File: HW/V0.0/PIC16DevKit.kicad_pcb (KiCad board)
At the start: 2 copper layers, 0 parts

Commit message: PIC16-DevKit-SCH-877 schematic update 5
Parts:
- added C1: 470uF, SAMPI:CAP_ELEC-8.3x8.3-DIA8.0, F.Cu at (77.6, 134.1)
- added C10: 10uF, SAMPI:CAP0603, F.Cu at (62.0, 146.1)
- added C11: 10uF, SAMPI:CAP0603, F.Cu at (65.7, 130.5)
- added C12: 22pF, SAMPI:CAP0603, F.Cu at (65.7, 133.1)
- added C13: 10uF, SAMPI:CAP0603, F.Cu at (65.7, 135.7)
- added C14: 100nF, SAMPI:CAP0603, F.Cu at (65.7, 138.3)
- added C15: 22pF, SAMPI:CAP0603, F.Cu at (89.7, 98.9)
- added C16: 22pF, SAMPI:CAP0603, F.Cu at (89.7, 101.5)
- added C17: 100nF, SAMPI:CAP0603, F.Cu at (89.7, 104.1)
- added C18: 100nF, SAMPI:CAP0603, F.Cu at (89.7, 106.7)
- added C19: 10uF, SAMPI:CAP0603, F.Cu at (89.7, 109.3)
- added C2: 220uF, SAMPI:CAP1411, F.Cu at (86.9, 144.4)
- added C20: 100nF, SAMPI:CAP0603, F.Cu at (93.4, 98.9)
- added C21: 10uF, SAMPI:CAP0603, F.Cu at (93.4, 101.5)
- added C22: 100nF, SAMPI:CAP0603, F.Cu at (99.3, 120.6)
- added C23: 100nF, SAMPI:CAP0603, F.Cu at (99.3, 123.2)
- added C24: 100nF, SAMPI:CAP0603, F.Cu at (99.3, 125.8)
- added C25: 100nF, SAMPI:CAP0603, F.Cu at (99.3, 128.5)
- added C26: 100nF, SAMPI:CAP0603, F.Cu at (99.3, 131.1)
- added C27: 10uF, SAMPI:CAP0603, F.Cu at (99.3, 133.7)
- added C28: 100nF, SAMPI:CAP0603, F.Cu at (99.3, 136.3)
- added C29: 10uF, SAMPI:CAP0603, F.Cu at (103.0, 120.6)
- added C3: 10uF/16V, SAMPI:CAP1206, F.Cu at (92.8, 140.3)
- added C30: 100nF, SAMPI:CAP0603, F.Cu at (103.0, 123.2)
- added C31: 100nF, SAMPI:CAP0603, F.Cu at (103.0, 125.8)
- added C32: 100nF, SAMPI:CAP0603, F.Cu at (103.0, 128.5)
- added C33: 100nF, SAMPI:CAP0603, F.Cu at (103.0, 131.1)
- added C34: 100nF, SAMPI:CAP0603, F.Cu at (103.0, 133.7)
- added C35: 100nF, SAMPI:CAP0603, F.Cu at (103.0, 136.3)
- added C36: 100nF, SAMPI:CAP0603, F.Cu at (106.7, 120.6)
- added C37: 100nF, SAMPI:CAP0603, F.Cu at (106.7, 123.2)
- added C4: 100nF, SAMPI:CAP0603, F.Cu at (62.0, 130.5)
- added C5: 100nF, SAMPI:CAP0603, F.Cu at (62.0, 133.1)
- added C6: 100nF, SAMPI:CAP0603, F.Cu at (62.0, 135.7)
- added C7: 10uF, SAMPI:CAP0603, F.Cu at (62.0, 138.3)
- added C8: 10uF, SAMPI:CAP0603, F.Cu at (62.0, 140.9)
- added C9: 10uF, SAMPI:CAP0603, F.Cu at (62.0, 143.5)
- added D1: 5V1, SAMPI:SOD80C-LL34, F.Cu at (86.9, 127.6)
- added D2: 200mA/0.2VF, Liem:SOD-123FL, F.Cu at (87.1, 136.5)
- added D3: TVS 5V, Triet_KiCAD_Fprint:SOT-143-TVS, F.Cu at (92.7, 136.8)
- added D4: 200mA/0.2VF, Liem:SOD-123FL, F.Cu at (87.1, 140.1)
- added D5: ULED, SAMPI:LED0603, F.Cu at (93.4, 104.1)
- added D6: TARGET, SAMPI:LED0603, F.Cu at (106.7, 125.8)
- added D7: BUSY, SAMPI:LED0603, F.Cu at (106.7, 128.5)
- added F1: 1A, SAMPI:FUSE1812, F.Cu at (80.3, 121.0)
- added F2: 750mA, SAMPI:FUSE1812, F.Cu at (80.3, 126.0)
- added J1: 9V-12V, Triet_KiCAD_Fprint:PJ-002AH-SMT-TR, F.Cu at (68.3, 121.5)
- added J2: USB4105-16P, Triet_KiCAD_Fprint:USB4105, F.Cu at (77.2, 144.4)
- added J3: EXP PORT, SAMPI:HDM1x10x2.54_TH_RA, F.Cu at (74.0, 108.6)
- added J4: PG ICSP, SAMPI:HD-1x6x1.27MM-TH, F.Cu at (116.9, 126.1)
- added L1: 10uH/1.8A, SAMPI:IND5852, F.Cu at (87.6, 122.3)
- added L2: 10uH/100mA, SAMPI:IND0805, F.Cu at (93.1, 120.0)
- added MD1: ARDUINO-UNO-R3, SAMPI:ARDUINO-UNO-R3, F.Cu at (75.9, 45.9)
- added Q1: SI2301DS, SAMPI:SOT23, F.Cu at (78.8, 116.2)
- added Q2: SI2302DS, SAMPI:SOT23, F.Cu at (83.4, 116.2)
- added Q3: SI2301DS, SAMPI:SOT23, F.Cu at (88.0, 116.2)
- added Q4: 2N3906, SAMPI:SOT23, F.Cu at (92.6, 116.2)
- added Q5: SI2302DS, SAMPI:SOT23, F.Cu at (99.7, 139.9)
- added Q6: SI2302DS, SAMPI:SOT23, F.Cu at (104.3, 139.9)
- added Q7: SI2302DS, SAMPI:SOT23, F.Cu at (108.9, 139.9)
- added R1: 52.3K, 1%, SAMPI:RES0603, F.Cu at (65.7, 140.9)
- added R10: 10K, 1%, SAMPI:RES0603, F.Cu at (69.4, 146.1)
- added R11: 330R, SAMPI:RES0603, F.Cu at (93.4, 106.7)
- added R12: 330R, SAMPI:RES0603, F.Cu at (93.4, 109.3)
- added R13: 330R, SAMPI:RES0603, F.Cu at (97.1, 98.9)
- added R14: 330R, SAMPI:RES0603, F.Cu at (97.1, 101.5)
- added R15: 330R, SAMPI:RES0603, F.Cu at (97.1, 104.1)
- added R16: 330R, SAMPI:RES0603, F.Cu at (97.1, 106.7)
- added R17: 330R, SAMPI:RES0603, F.Cu at (97.1, 109.3)
- added R18: 10K, SAMPI:RES0603, F.Cu at (100.9, 98.9)
- added R19: 330R, SAMPI:RES0603, F.Cu at (100.9, 101.5)
- added R2: 10K, 1%, SAMPI:RES0603, F.Cu at (65.7, 143.5)
- added R20: 330R, SAMPI:RES0603, F.Cu at (100.9, 104.1)
- added R21: 5.1K, 1%, SAMPI:RES0603, F.Cu at (100.9, 106.7)
- added R22: 5.1K, 1%, SAMPI:RES0603, F.Cu at (100.9, 109.3)
- added R23: 10K, SAMPI:RES0603, F.Cu at (106.7, 131.1)
- added R24: 330R, SAMPI:RES0603, F.Cu at (106.7, 133.7)
- added R25: 330R, SAMPI:RES0603, F.Cu at (106.7, 136.3)
- added R26: 10K, SAMPI:RES0603, F.Cu at (110.4, 120.6)
- added R27: 5.1K, 1%, SAMPI:RES0603, F.Cu at (110.4, 123.2)
- added R28: 5.1K, 1%, SAMPI:RES0603, F.Cu at (110.4, 125.8)
- added R29: 330R, SAMPI:RES0603, F.Cu at (110.4, 128.5)
- added R3: 100K, SAMPI:RES0603, F.Cu at (65.7, 146.1)
- added R30: 5.1K, 1%, SAMPI:RES0603, F.Cu at (110.4, 131.1)
- added R31: 5.1K, 1%, SAMPI:RES0603, F.Cu at (110.4, 133.7)
- added R4: 100K, SAMPI:RES0603, F.Cu at (69.4, 130.5)
- added R5: 191K, 1%, SAMPI:RES0603, F.Cu at (69.4, 133.1)
- added R6: 5.1K, 1%, SAMPI:RES0603, F.Cu at (69.4, 135.7)
- added R7: 5.1K, 1%, SAMPI:RES0603, F.Cu at (69.4, 138.3)
- added R8: 100K, SAMPI:RES0603, F.Cu at (69.4, 140.9)
- added R9: 100K, SAMPI:RES0603, F.Cu at (69.4, 143.5)
- added SW1: UBT, Triet_KiCAD_Fprint:SW_2P_3.5x6, F.Cu at (122.0, 100.1)
- added SW2: RESET, Triet_KiCAD_Fprint:SW_2P_3.5x6, F.Cu at (117.3, 121.8)
- added U1: 3.3V/300mA, Triet_KiCAD_Fprint:MIC5504_SOT, F.Cu at (92.3, 144.0)
- added U10: 20MHz, SAMPI:CDFN3225-4LD-PL-1, F.Cu at (130.7, 114.0)
- added U2: MT1470, SAMPI:SOT-23-6_MCHP, F.Cu at (86.4, 131.9)
- added U3: MT3608, SAMPI:SOT-23-6_MCHP, F.Cu at (91.1, 131.9)
- added U4: PIC16F877A, SAMPI:TQFP44-10x10-P0.8, F.Cu at (109.8, 104.7)
- added U5: PIC32MM, Triet_KiCAD_Fprint:UQFN28-EP, F.Cu at (115.9, 131.5)
- added U6: SN74LVC1T45, SAMPI:SOT-23-6_MCHP, F.Cu at (99.8, 116.6)
- added U7: SN74LVC1T45, SAMPI:SOT-23-6_MCHP, F.Cu at (104.5, 116.6)
- added U8: SN74LVC1T45, SAMPI:SOT-23-6_MCHP, F.Cu at (109.2, 116.6)
- added U9: SN74LVC1T45, SAMPI:SOT-23-6_MCHP, F.Cu at (113.9, 116.6)

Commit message: PIC16-DevKit-SCH-877 schematic update 6
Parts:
- removed SW1: UBT, Triet_KiCAD_Fprint:SW_2P_3.5x6
- removed SW2: RESET, Triet_KiCAD_Fprint:SW_2P_3.5x6
- removed U5: PIC32MM, Triet_KiCAD_Fprint:UQFN28-EP
- added BT1: MODE, Liem:SW6x6-G, F.Cu at (66.8, 55.1)
- added BT2: UBT, Liem:SW6x6-G, F.Cu at (66.8, 47.1)
- added C38: 100nF, SAMPI:CAP0603, F.Cu at (166.1, 123.0)
- added C39: 100nF, SAMPI:CAP0603, F.Cu at (82.1, 71.4)
- added R32: 10K, 1%, SAMPI:RES0603, F.Cu at (82.1, 74.0)
- added R33: 10K, 1%, SAMPI:RES0603, F.Cu at (82.1, 76.6)
- added U11: PIC32MM0064GPM028, SAMPI:UQFN28-4x4-EP, F.Cu at (76.9, 67.6)
- D2, D4: footprint Liem:SOD-123FL -> SAMPI:SOD-123FL
- D3: footprint Triet_KiCAD_Fprint:SOT-143-TVS -> SAMPI:SOT143B_NEXT
- F2: value 750mA -> 500mA
- J1: footprint Triet_KiCAD_Fprint:PJ-002AH-SMT-TR -> SAMPI:PJ-002AH-SMT
- J2: value USB4105-16P -> USB C; footprint Triet_KiCAD_Fprint:USB4105 -> SAMPI:USB4105
- J3: footprint SAMPI:HDM1x10x2.54_TH_RA -> SAMPI:HDM1x10x2.54_TH
- L1: value 10uH/1.8A -> 10uH/1.4A
- Q1, Q3: value SI2301DS -> SI2301
- Q2, Q5, Q6, Q7: value SI2302DS -> SI2302
- U1: value 3.3V/300mA -> LDO 3.3V/300mA; footprint Triet_KiCAD_Fprint:MIC5504_SOT -> SAMPI:SOT-23-5_MCHP
- moved J2 79.7 mm to (64.3, 65.7), turned to -90 degrees
- moved J4 76.3 mm to (76.4, 61.4)
- moved J3 59.3 mm to (123.0, 75.1), turned to 90 degrees
- moved F2 54.6 mm to (62.8, 74.3), turned to -90 degrees
- moved R17 48.6 mm to (119.5, 66.1)
- moved R20 44.6 mm to (119.6, 63.6)
- moved R16 44.1 mm to (119.4, 68.7)
- moved R12 40.0 mm to (119.4, 78.9)
- moved R15 39.6 mm to (119.3, 71.3)
- moved F1 39.2 mm to (76.1, 82.1), turned to -90 degrees
- moved R11 36.2 mm to (119.4, 81.5)
- moved R14 35.6 mm to (119.4, 73.7)
- moved J1 35.0 mm to (66.1, 86.5), turned to -90 degrees
- moved U4 32.7 mm to (107.2, 72.2)
- moved R13 31.9 mm to (119.6, 76.2)
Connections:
- MD1 pad 15: /TARGET MCU/RXD -> /PROGRAMMER/~{TG_RXD}
- MD1 pad 16: /TARGET MCU/TXD -> /PROGRAMMER/~{TG_TXD}
- MD1 pad 3: /TARGET MCU/~{MCLR} -> /PROGRAMMER/~{TG_MCLR}
- MD1 pad 31: /TARGET MCU/SDA -> /PROGRAMMER/TG_SDA
- MD1 pad 32: /TARGET MCU/SCL -> /PROGRAMMER/TG_SCL
- R21 pad 2: /TARGET MCU/SCL -> /PROGRAMMER/TG_SCL
- R22 pad 2: /TARGET MCU/SDA -> /PROGRAMMER/TG_SDA
- R6 pad 1: Net-(J2-CC1) -> Net-(J2-CC2)
- R7 pad 1: Net-(J2-CC2) -> Net-(J2-CC1)
- U4 pad 1: /TARGET MCU/RXD -> /PROGRAMMER/~{TG_RXD}
- U4 pad 16: /TARGET MCU/PGC -> /PROGRAMMER/~{TG_PGC}
- U4 pad 17: /TARGET MCU/PGD -> /PROGRAMMER/~{TG_PGD}
- U4 pad 18: /TARGET MCU/~{MCLR} -> /PROGRAMMER/~{TG_MCLR}
- U4 pad 37: /TARGET MCU/SCL -> /PROGRAMMER/TG_SCL
- U4 pad 42: /TARGET MCU/SDA -> /PROGRAMMER/TG_SDA
- U4 pad 44: /TARGET MCU/TXD -> /PROGRAMMER/~{TG_TXD}
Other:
- board outline added: 68.8 x 54 mm
- copper layers 2 -> 4

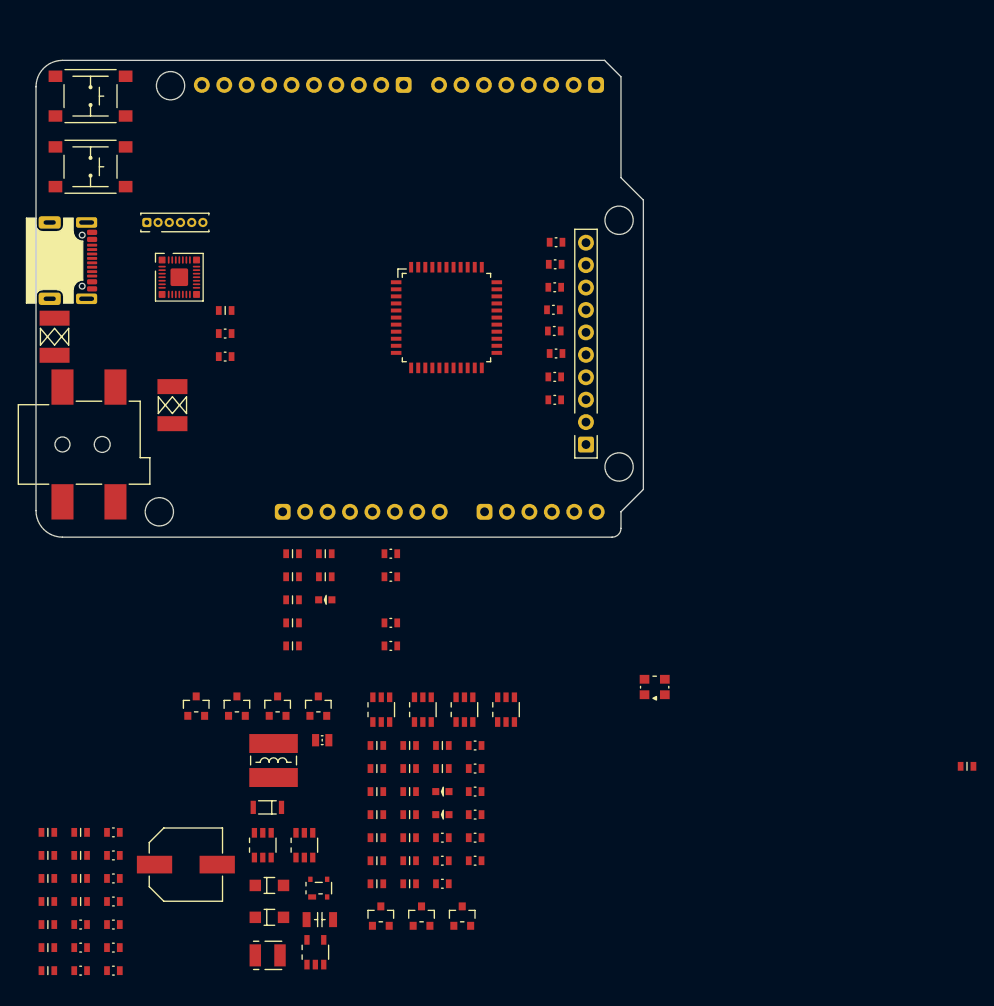
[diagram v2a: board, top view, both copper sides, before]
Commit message: PIC16-DevKit-SCH-877 schematic update 7
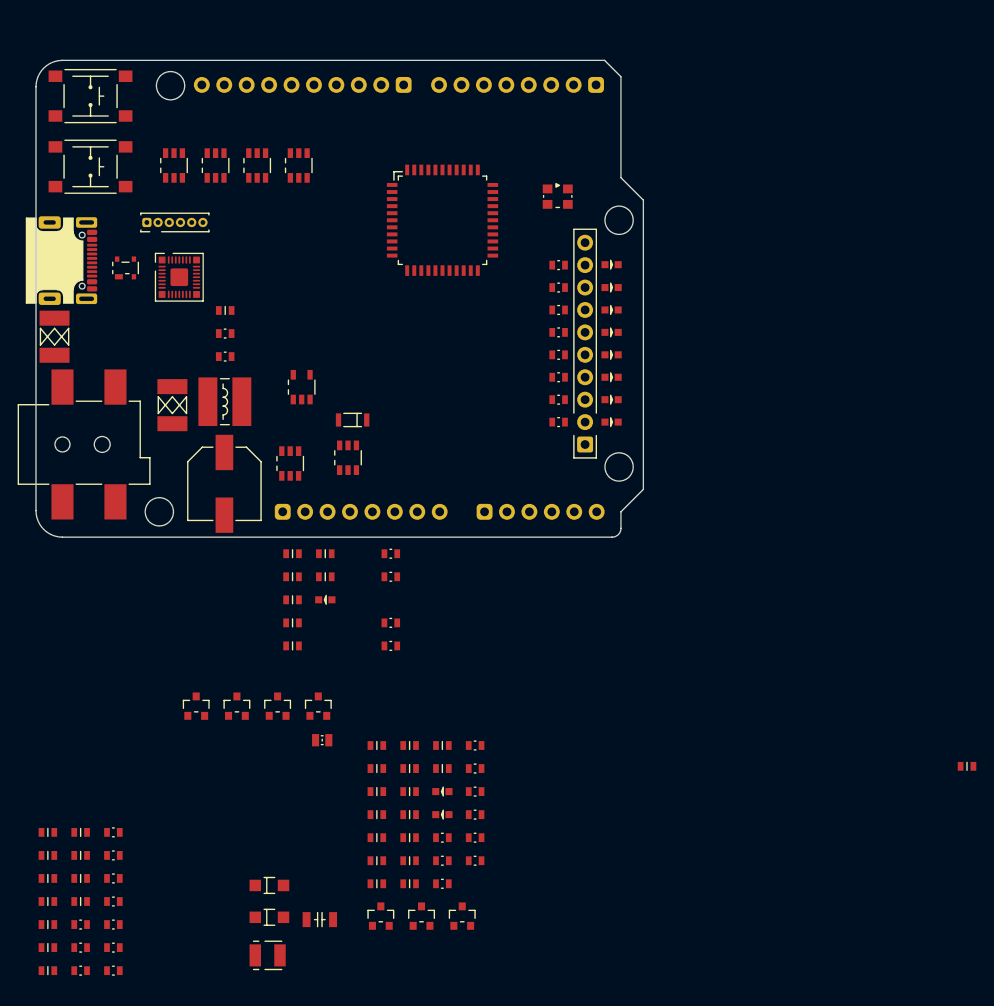
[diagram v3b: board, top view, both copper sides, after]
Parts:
- added D10: RD5, SAMPI:LED0603, F.Cu at (125.9, 71.3)
- added D11: RD4, SAMPI:LED0603, F.Cu at (125.9, 73.8)
- added D12: RD3, SAMPI:LED0603, F.Cu at (125.9, 76.4)
- added D13: RD2, SAMPI:LED0603, F.Cu at (125.9, 78.9)
- added D14: RD1, SAMPI:LED0603, F.Cu at (125.9, 81.5)
- added D15: RD0, SAMPI:LED0603, F.Cu at (125.9, 84.0)
- added D8: RD7, SAMPI:LED0603, F.Cu at (125.9, 66.2)
- added D9: RD6, SAMPI:LED0603, F.Cu at (125.9, 68.8)
- moved D3 73.6 mm to (70.8, 66.5)
- moved U6 65.9 mm to (76.3, 54.9)
- moved U7 65.9 mm to (81.0, 54.9)
- moved U9 65.9 mm to (90.4, 54.9)
- moved U8 65.9 mm to (85.7, 54.9)
- moved U1 64.0 mm to (90.8, 80.0)
- moved U10 56.7 mm to (119.8, 58.4), turned to 180 degrees
- moved D1 44.9 mm to (96.5, 83.8)
- moved U2 44.9 mm to (96.0, 88.0)
- moved C1 43.3 mm to (82.0, 91.0), turned to -90 degrees
- moved U3 43.3 mm to (89.5, 88.7)
- moved L1 41.0 mm to (82.1, 81.7), turned to -90 degrees
- moved U4 11.0 mm to (106.7, 61.1)
- moved R14 2.74 mm to (119.9, 76.4)
- moved R13 2.71 mm to (119.9, 78.9)
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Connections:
- J3 pad 1: GND -> +VDDTG
- J3 pad 10: Net-(J3-Pad10) -> GND
- J3 pad 2: +VDDTG -> Net-(D15-PadA)
- J3 pad 3: Net-(J3-Pad3) -> Net-(D14-PadA)
- J3 pad 4: Net-(J3-Pad4) -> Net-(D13-PadA)
- J3 pad 5: Net-(J3-Pad5) -> Net-(D12-PadA)
- J3 pad 6: Net-(J3-Pad6) -> Net-(D11-PadA)
- J3 pad 7: Net-(J3-Pad7) -> Net-(D10-PadA)
- J3 pad 8: Net-(J3-Pad8) -> Net-(D9-PadA)
- J3 pad 9: Net-(J3-Pad9) -> Net-(D8-PadA)
- R11 pad 2: Net-(J3-Pad3) -> Net-(D15-PadA)
- R12 pad 2: Net-(J3-Pad4) -> Net-(D14-PadA)
- R13 pad 2: Net-(J3-Pad5) -> Net-(D13-PadA)
- R14 pad 2: Net-(J3-Pad6) -> Net-(D12-PadA)
- R15 pad 2: Net-(J3-Pad7) -> Net-(D11-PadA)
- R16 pad 2: Net-(J3-Pad8) -> Net-(D10-PadA)
- R17 pad 2: Net-(J3-Pad9) -> Net-(D9-PadA)
- R20 pad 2: Net-(J3-Pad10) -> Net-(D8-PadA)

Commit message: PIC16-DevKit-PCB-877 layout update 1
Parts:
- moved C9 90.6 mm to (87.5, 56.6)
- moved D4 89.9 mm to (77.2, 50.7)
- moved R9 87.5 mm to (79.1, 56.6)
- moved R23 85.4 mm to (72.4, 52.9), turned to -90 degrees
- moved C10 84.6 mm to (72.2, 62.2)
- moved R8 84.5 mm to (75.3, 56.6), turned to 180 degrees
- moved C35 84.1 mm to (98.3, 52.3), turned to 90 degrees
- moved C34 81.7 mm to (111.2, 52.3), turned to 90 degrees
- moved Q7 80.1 mm to (101.5, 60.2), turned to 180 degrees
- moved Q6 79.8 mm to (105.5, 60.2), turned to 180 degrees
- moved C33 78.8 mm to (105.6, 52.3), turned to 90 degrees
- moved C24 78.2 mm to (125.9, 52.3), turned to 90 degrees
- moved R25 77.9 mm to (85.1, 61.4)
- moved C38 77.8 mm to (98.1, 85.1), turned to -90 degrees
- moved R31 76.8 mm to (101.5, 57.4), turned to 180 degrees
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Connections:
- D5 pad A: Net-(D5-PadA) -> /TARGET MCU/ULED
- D5 pad K: GND -> Net-(D5-PadK)
- R19 pad 1: /TARGET MCU/ULED -> Net-(D5-PadK)
- R19 pad 2: Net-(D5-PadA) -> GND
- U11 pad 6: unconnected-(U11-OSC1/CLKI/AN5/RP3/OCM1C/RA2-Pad6) -> /POWER/VPP_EN
- U11 pad 7: unconnected-(U11-OSC2/CLKO/AN6/C3IND/RP4/OCM1D/RA3-Pad7) -> /POWER/~{VTG_EN}
- U11 pad 8: unconnected-(U11-SOSCI/AN7/RP10/OCM3C/RB4-Pad8) -> /PROGRAMMER/LED_TGRDY
- U11 pad 9: unconnected-(U11-SOSCO/SCLKI/RP5/PWRLCLK/OCM3D/RA4-Pad9) -> /PROGRAMMER/LED_BUSY
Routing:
- net VDC: track 0.00 -> 30.5 mm
- net Net-(F2-Pad1): track 0.00 -> 14.7 mm
- net /POWER/USB_P: track 0.00 -> 12.4 mm
- net /POWER/USB_N: track 0.00 -> 11.8 mm
- net Net-(F1-Pad1): track 0.00 -> 11.1 mm
- net +5V: track 0.00 -> 9.81 mm
- net +3.3V: track 0.00 -> 9.78 mm
- net /PROGRAMMER/LED_BUSY: track 0.00 -> 6.57 mm
- net Net-(U11-VCAP): track 0.00 -> 5.49 mm
- net Net-(U2-SW): track 0.00 -> 4.99 mm
- net /PROGRAMMER/LED_TGRDY: track 0.00 -> 4.90 mm
- net Net-(D12-PadA): track 0.00 -> 4.53 mm
- net Net-(D13-PadA): track 0.00 -> 4.53 mm
- net Net-(D11-PadA): track 0.00 -> 4.53 mm
- net Net-(D9-PadA): track 0.00 -> 4.52 mm
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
